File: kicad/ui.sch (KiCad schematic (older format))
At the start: 18 parts, among them J1501 NHD-4.3-480272FT-CTXL-T, J1502 Conn_01x02, SW1501 SW_Push, SW1502 SW_Push, SW1503 SW_Push, SW1504 SW_Push, U1501 PAM8301

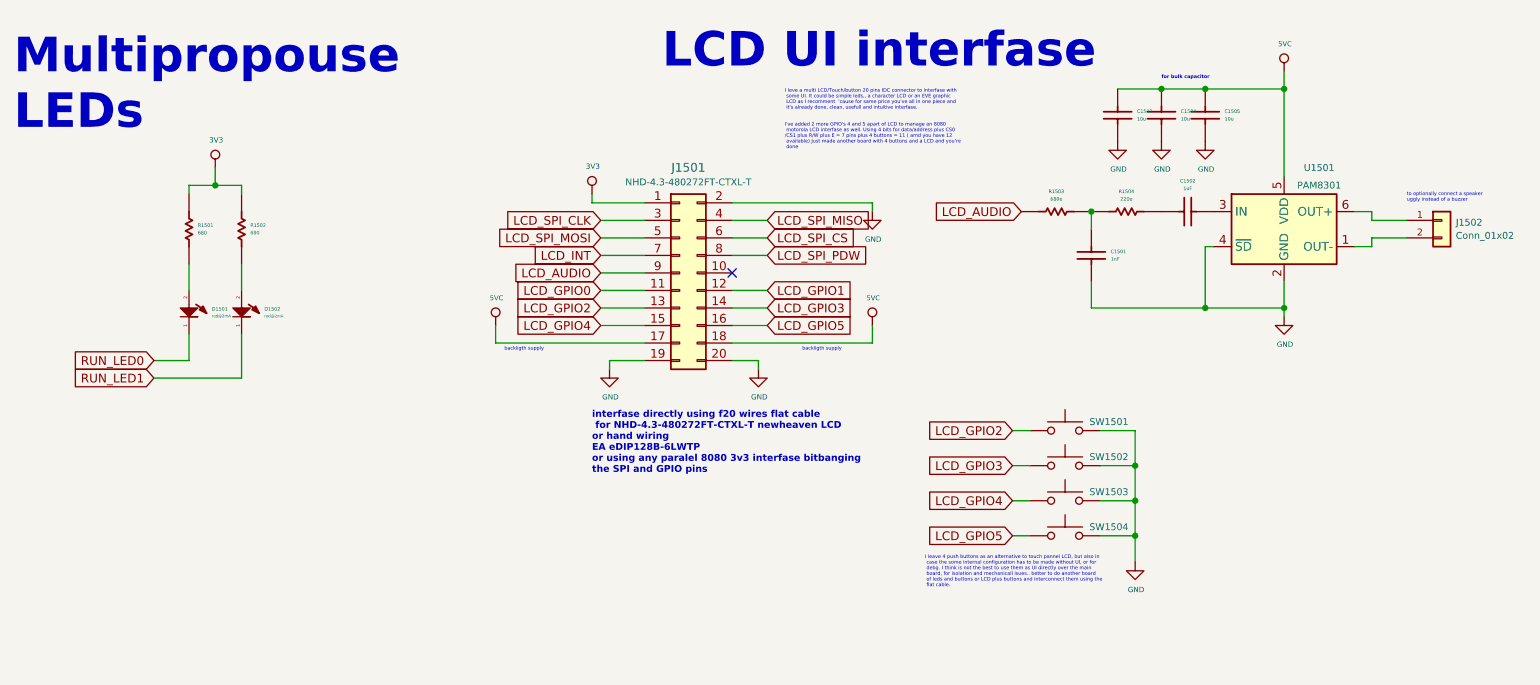
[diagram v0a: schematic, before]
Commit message: changing single row terminal block to double row
I've changed to double row all the connectors, RJ45 and terminal blocks,
I saves spaces and also make it more intuitive related to user
interface..lets go
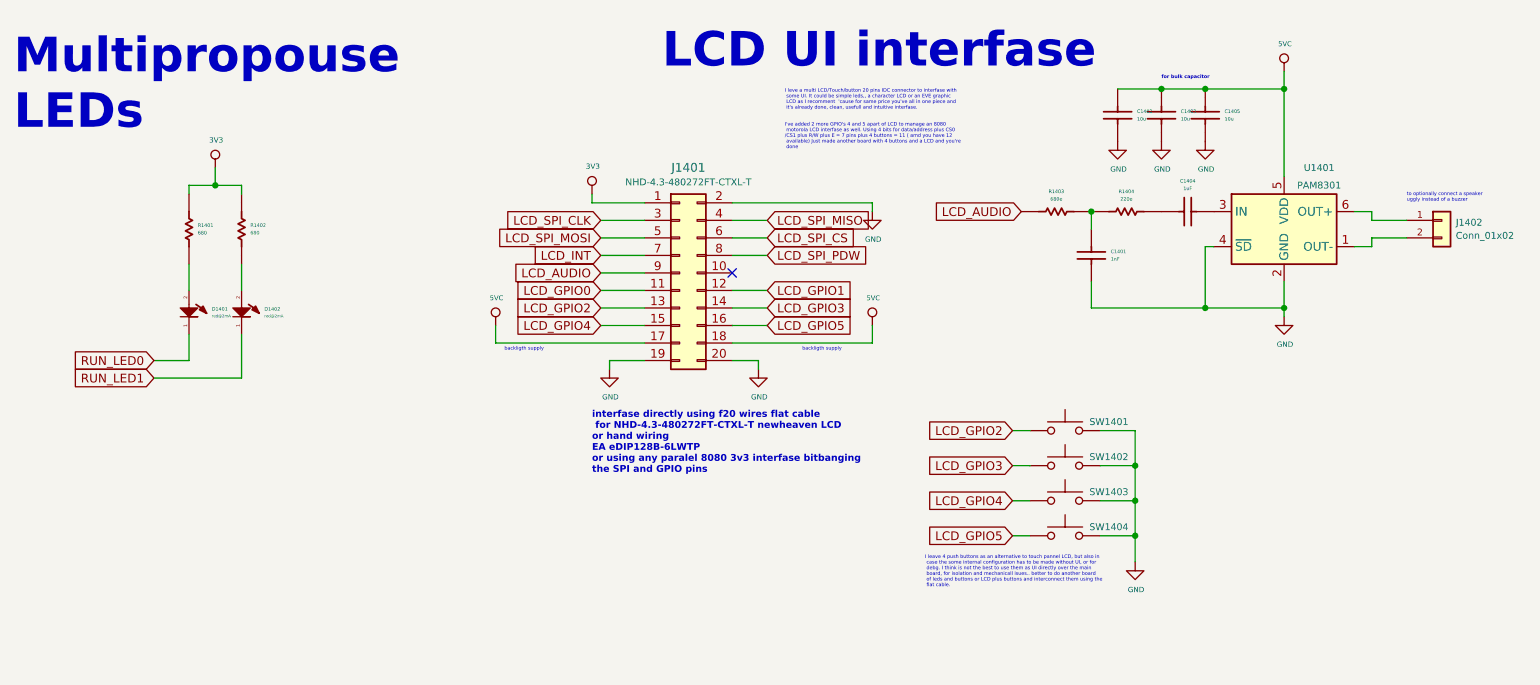
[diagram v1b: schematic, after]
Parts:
- renumbered C1501 to C1401, C1503 to C1402, C1504 to C1403, C1502 to C1404, C1505 to C1405, D1501 to D1401, D1502 to D1402, J1501 to J1401, J1502 to J1402, R1501 to R1401, R1502 to R1402, R1503 to R1403, R1504 to R1404, SW1501 to SW1401, SW1502 to SW1402, SW1503 to SW1403, SW1504 to SW1404, U1501 to U1401

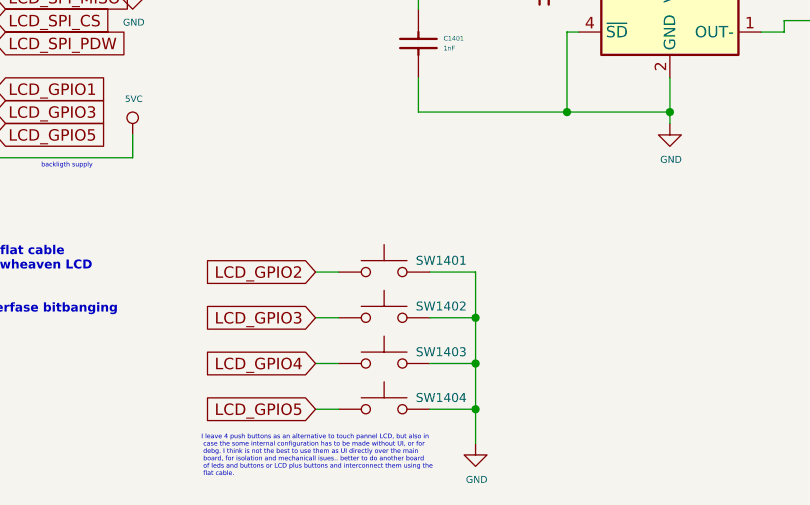
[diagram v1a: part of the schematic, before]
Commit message: added some 3d models, elminating 15vc and 2 lems
I've elminated 15vc 'cause I don't use these voltage, so I'd change 20w
15v heating power to 10w 5v more efficiency voltage to drive 3.3 and
1.2v to the core and logic. I've also elminated 2 LEMS 'cause space..
even thought there remain 3 for each motor.. more than necesary...keep
going
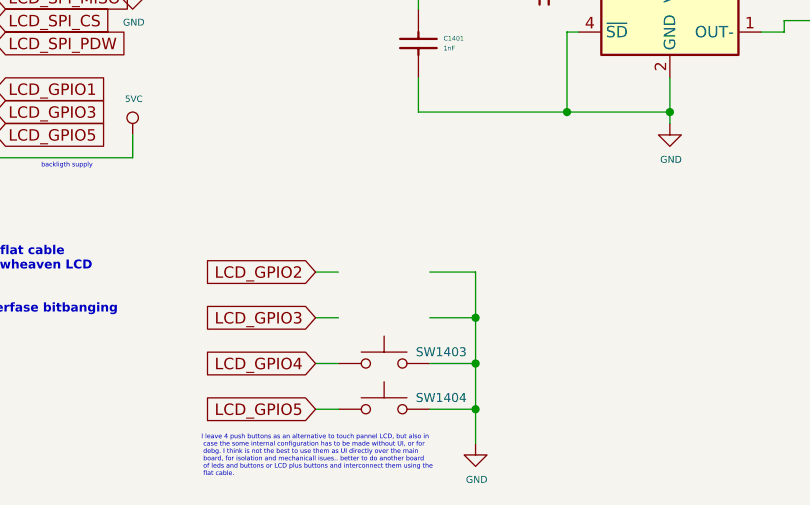
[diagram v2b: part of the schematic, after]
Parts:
- removed SW1401, SW1402: SW_Push, Button_Switch_SMD:SW_SPST_PTS645, symbol servo:SW_Push
- J1401: footprint Connector_IDC:IDC-Header_2x10_P2.54mm_Vertical -> servo:HD-4.3-480272
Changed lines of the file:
@@
 $Descr A4 11693 8268
 encoding utf-8
-Sheet 15 18
+Sheet 14 18
 Title "clk"
 Date "2020-01-09"
@@
 NoConn ~ 5450 2050
 $Comp
-L servo:SW_Push SW1401
-U 1 1 5EF4D647
-P 7350 2950
-F 0 "SW1401" H 7600 3000 39  0000 C CNN
-F 1 "SW_Push" H 7350 3136 39  0001 C CNN
-F 2 "Button_Switch_SMD:SW_SPST_PTS645" H 7350 3150 50  0001 C CNN
-F 3 "" H 7350 3150 50  0001 C CNN
-	1    7350 2950
-	1    0    0    -1
-$EndComp
-$Comp
-L servo:SW_Push SW1402
-U 1 1 5EF4D88E
-P 7350 3150
-F 0 "SW1402" H 7600 3200 39  0000 C CNN
-F 1 "SW_Push" H 7350 3336 39  0001 C CNN
-F 2 "Button_Switch_SMD:SW_SPST_PTS645" H 7350 3350 50  0001 C CNN
-F 3 "" H 7350 3350 50  0001 C CNN
-	1    7350 3150
-	1    0    0    -1
-$EndComp
-$Comp
 L servo:SW_Push SW1403
 U 1 1 5EF4E22E
@@
 F 0 "J1401" H 5200 2651 50  0000 C CNN
 F 1 "NHD-4.3-480272FT-CTXL-T" H 5200 2568 39  0000 C CNN
-F 2 "Connector_IDC:IDC-Header_2x10_P2.54mm_Vertical" H 5150 2050 50  0001 C CNN
+F 2 "servo:HD-4.3-480272" H 5150 2050 50  0001 C CNN
 F 3 "../doc/datasheets/NHD-4.3-480272FT-CTXL-T.pdf" H 5200 2550 50  0001 C CNN
 	1    5150 2050

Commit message: keep placing
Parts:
- J1402: footprint Connector_PinHeader_2.54mm:PinHeader_1x02_P2.54mm_Vertical_SMD_Pin1Left -> Connector_Molex:Molex_KK-254_AE-6410-02A_1x02_P2.54mm_Vertical
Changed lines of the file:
@@
 F 0 "J1402" H 9580 1738 39  0000 L CNN
 F 1 "Conn_01x02" H 9580 1663 39  0000 L CNN
-F 2 "Connector_PinHeader_2.54mm:PinHeader_1x02_P2.54mm_Vertical_SMD_Pin1Left" H 9500 1750 50  0001 C CNN
+F 2 "Connector_Molex:Molex_KK-254_AE-6410-02A_1x02_P2.54mm_Vertical" H 9500 1750 50  0001 C CNN
 F 3 "~" H 9500 1750 50  0001 C CNN
 	1    9500 1750

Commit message: beginine routing... far far away
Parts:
- removed C1405: 10u, servo:C_0603_1608Metric, symbol servo:Capacitor
- removed SW1403, SW1404: SW_Push, Button_Switch_SMD:SW_SPST_PTS645, symbol servo:SW_Push
- J1401: footprint servo:HD-4.3-480272 -> servo:idc2x10_smd
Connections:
- wire segments 67 -> 66
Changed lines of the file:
@@
 NoConn ~ 5450 2050
-$Comp
-L servo:SW_Push SW1403
-U 1 1 5EF4E22E
-P 7350 3350
-F 0 "SW1403" H 7600 3400 39  0000 C CNN
-F 1 "SW_Push" H 7350 3536 39  0001 C CNN
-F 2 "Button_Switch_SMD:SW_SPST_PTS645" H 7350 3550 50  0001 C CNN
-F 3 "" H 7350 3550 50  0001 C CNN
-	1    7350 3350
-	1    0    0    -1
-$EndComp
-$Comp
-L servo:SW_Push SW1404
-U 1 1 5EF4EBD2
-P 7350 3550
-F 0 "SW1404" H 7600 3600 39  0000 C CNN
-F 1 "SW_Push" H 7350 3736 39  0001 C CNN
-F 2 "Button_Switch_SMD:SW_SPST_PTS645" H 7350 3750 50  0001 C CNN
-F 3 "" H 7350 3750 50  0001 C CNN
-	1    7350 3550
-	1    0    0    -1
-$EndComp
 $Comp
 L servo:GND #PWR?
@@
 F 0 "J1401" H 5200 2651 50  0000 C CNN
 F 1 "NHD-4.3-480272FT-CTXL-T" H 5200 2568 39  0000 C CNN
-F 2 "servo:HD-4.3-480272" H 5150 2050 50  0001 C CNN
+F 2 "servo:idc2x10_smd" H 5150 2050 50  0001 C CNN
 F 3 "../doc/datasheets/NHD-4.3-480272FT-CTXL-T.pdf" H 5200 2550 50  0001 C CNN
 	1    5150 2050
@@
 Wire Wire Line
 	8600 1500 8600 1000
-$Comp
-L servo:Capacitor C?
-U 1 1 618D8220
-P 8150 1200
-AR Path="/5E092156/618D8220" Ref="C?"  Part="1"
-AR Path="/5E72D841/618D8220" Ref="C1405"  Part="1"
-F 0 "C1405" V 8222 1090 20  0000 R CNN
-F 1 "10u" V 8179 1090 20  0000 R CNN
-F 2 "servo:C_0603_1608Metric" H 8150 1100 60  0001 C CNN
-F 3 "" H 8150 1200 60  0000 C CNN
-	1    8150 1200
-	0    -1   -1   0
-$EndComp
-Wire Wire Line
-	8150 1000 8600 1000
 Connection ~ 8600 1000
 Wire Wire Line
 	8600 1000 8600 900
-$Comp
-L servo:GND #PWR?
-U 1 1 618DC4D7
-P 8150 1300
-AR Path="/5DCD812E/618DC4D7" Ref="#PWR?"  Part="1"
-AR Path="/5EAA846A/618DC4D7" Ref="#PWR?"  Part="1"
-AR Path="/5F1E3CD5/618DC4D7" Ref="#PWR?"  Part="1"
-AR Path="/5DD76B18/618DC4D7" Ref="#PWR?"  Part="1"
-AR Path="/5E72D841/618DC4D7" Ref="#PWR01409"  Part="1"
-F 0 "#PWR01409" H 8155 1151 20  0001 C CNN
-F 1 "GND" H 8155 1142 30  0000 C CNN
-F 2 "" H 8150 1300 70  0000 C CNN
-F 3 "" H 8150 1300 70  0000 C CNN
-	1    8150 1300
-	1    0    0    -1
-$EndComp
 $Comp
 L servo:Capacitor C?
@@
 	1    0    0    -1
 $EndComp
-Wire Wire Line
-	8150 1000 7900 1000
-Connection ~ 8150 1000
 Connection ~ 7900 1000
 Wire Wire Line
@@
 Text Notes 7900 950  0    20   ~ 4
 for bulk capacitor
+Wire Wire Line
+	7900 1000 8600 1000
 $EndSCHEMATC

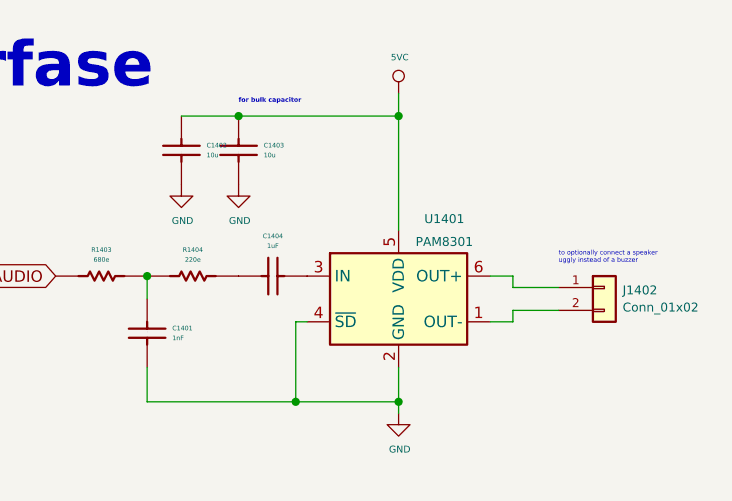
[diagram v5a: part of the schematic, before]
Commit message: ROUTING DONE!!!!!!!!!!!!!!!!!!!!!!!!!
ok, but....I need to improve all the nets, get them wider and so, but at
least all nets were routed to the uController.. it was more difucult
than I ever imagine... it tooks me 1 week only the uC coarse layout..
very very complex.. a lot of traces.. and with NO blind vias.. so it'll
be cheaper and any prototype manufacturer could do the board, and it'll
be more reliable..AND I'd test all nets on the board it it has at least
one via, or rout alongside top or bottom, so it's all the nets.. for
debug, it's very important...
lets do some improvement...
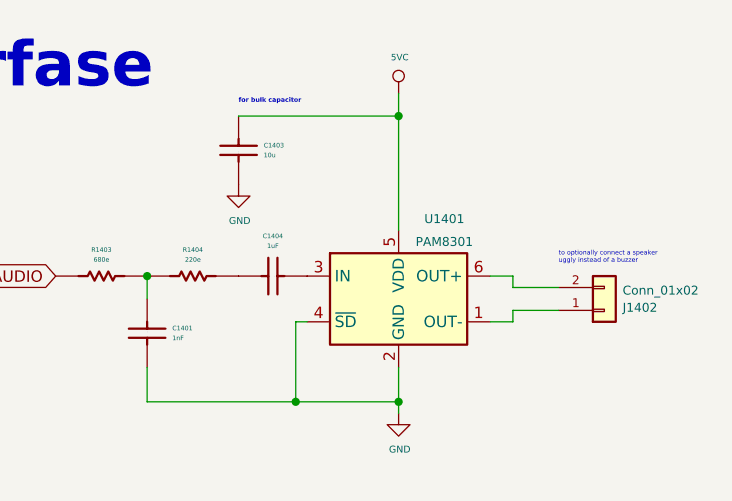
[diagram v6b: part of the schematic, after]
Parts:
- removed C1402: 10u, servo:C_0603_1608Metric, symbol servo:Capacitor
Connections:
- wire segments 66 -> 65
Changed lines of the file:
@@
 $EndComp
-$Comp
-L servo:Capacitor C?
-U 1 1 618DEC86
-P 7650 1200
-AR Path="/5E092156/618DEC86" Ref="C?"  Part="1"
-AR Path="/5E72D841/618DEC86" Ref="C1402"  Part="1"
-F 0 "C1402" V 7722 1090 20  0000 R CNN
-F 1 "10u" V 7679 1090 20  0000 R CNN
-F 2 "servo:C_0603_1608Metric" H 7650 1100 60  0001 C CNN
-F 3 "" H 7650 1200 60  0000 C CNN
-	1    7650 1200
-	0    -1   -1   0
-$EndComp
-$Comp
-L servo:GND #PWR?
-U 1 1 618DEC8D
-P 7650 1300
-AR Path="/5DCD812E/618DEC8D" Ref="#PWR?"  Part="1"
-AR Path="/5EAA846A/618DEC8D" Ref="#PWR?"  Part="1"
-AR Path="/5F1E3CD5/618DEC8D" Ref="#PWR?"  Part="1"
-AR Path="/5DD76B18/618DEC8D" Ref="#PWR?"  Part="1"
-AR Path="/5E72D841/618DEC8D" Ref="#PWR01406"  Part="1"
-F 0 "#PWR01406" H 7655 1151 20  0001 C CNN
-F 1 "GND" H 7655 1142 30  0000 C CNN
-F 2 "" H 7650 1300 70  0000 C CNN
-F 3 "" H 7650 1300 70  0000 C CNN
-	1    7650 1300
-	1    0    0    -1
-$EndComp
-Connection ~ 7900 1000
-Wire Wire Line
-	7900 1000 7650 1000
 $Comp
 L servo:Conn_01x02 J1402
 U 1 1 618ED4ED
-P 9500 1750
-F 0 "J1402" H 9580 1738 39  0000 L CNN
-F 1 "Conn_01x02" H 9580 1663 39  0000 L CNN
-F 2 "Connector_Molex:Molex_KK-254_AE-6410-02A_1x02_P2.54mm_Vertical" H 9500 1750 50  0001 C CNN
-F 3 "~" H 9500 1750 50  0001 C CNN
-	1    9500 1750
-	1    0    0    -1
+P 9500 1850
+F 0 "J1402" H 9580 1838 39  0000 L CNN
+F 1 "Conn_01x02" H 9580 1763 39  0000 L CNN
+F 2 "Connector_Molex:Molex_KK-254_AE-6410-02A_1x02_P2.54mm_Vertical" H 9500 1850 50  0001 C CNN
+F 3 "~" H 9500 1850 50  0001 C CNN
+	1    9500 1850
+	1    0    0    1
 $EndComp
 Text Notes 7900 950  0    20   ~ 4

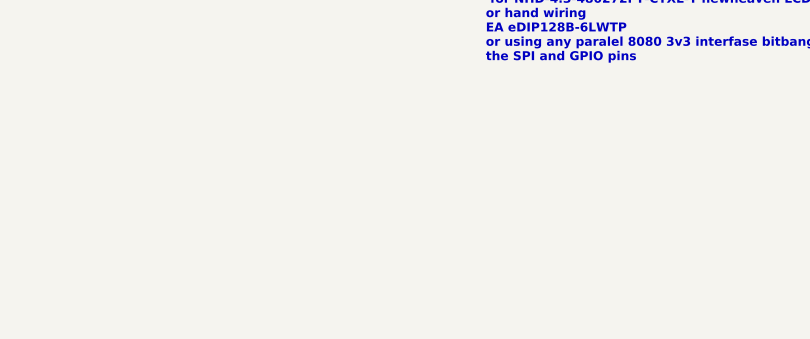
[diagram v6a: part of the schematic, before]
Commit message: add optional mounting case
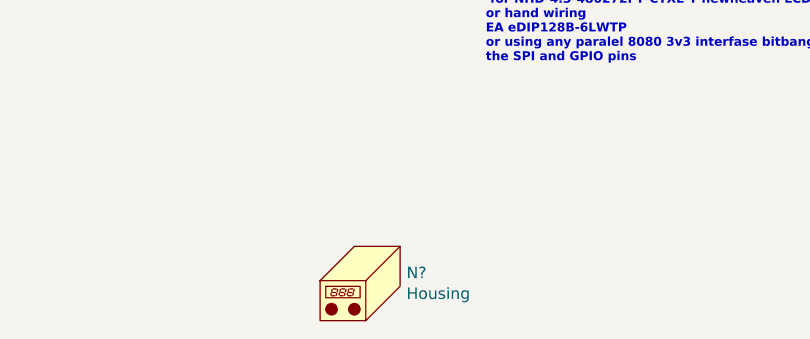
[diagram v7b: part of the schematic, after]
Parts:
- added N?: Housing, servo:case, symbol Mechanical:Housing
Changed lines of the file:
@@
 Wire Wire Line
 	7900 1000 8600 1000
+$Comp
+L Mechanical:Housing N?
+U 1 1 5E32F2AD
+P 4150 4150
+F 0 "N?" H 4303 4184 50  0000 L CNN
+F 1 "Housing" H 4303 4093 50  0000 L CNN
+F 2 "servo:case" H 4200 4200 50  0001 C CNN
+F 3 "~" H 4200 4200 50  0001 C CNN
+	1    4150 4150
+	1    0    0    -1
+$EndComp
 $EndSCHEMATC

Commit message: improvement...
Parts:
- gave numbers to parts that had none: 1
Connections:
- net labels added: speaker+, speaker-
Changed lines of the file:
@@
 	7900 1000 8600 1000
 $Comp
-L Mechanical:Housing N?
+L Mechanical:Housing N1401
 U 1 1 5E32F2AD
 P 4150 4150
-F 0 "N?" H 4303 4184 50  0000 L CNN
+F 0 "N1401" H 4303 4184 50  0000 L CNN
 F 1 "Housing" H 4303 4093 50  0000 L CNN
 F 2 "servo:case" H 4200 4200 50  0001 C CNN
@@
 	1    0    0    -1
 $EndComp
+Text Label 9200 1750 0    20   ~ 0
+speaker+
+Text Label 9200 1850 0    20   ~ 0
+speaker-
 $EndSCHEMATC
